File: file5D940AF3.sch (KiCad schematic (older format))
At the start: 42 parts, among them CN1 KEYBOARD_20PIN_MALE, CN2 USER_PORT_CON, CN4 SERIAL_BUS_CON, CN8 CONTROL_PORT, CN9 CONTROL_PORT, U1 CIA_U1, U2 CIA_U2, U20 556, U27 7408_U27, U28 4066_U28, U7 6510_MPU, U8 7406N

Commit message: schematics update
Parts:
- removed RP3: R_US_ARRAY, Resistor_THT:R_Array_SIP8, symbol KU-schematics-library:R_US_ARRAY
- added FB5: FERRITE_NARROW, KU-14194HB-RevB-KiCad:RECTIFIER, symbol KU-schematics-library:FERRITE_NARROW
- added RP3: R_ARRAY_7WAY_US, KU-14194HB-RevB-KiCad:RP_ARRAY_7WAY, symbol KU-schematics-library:R_ARRAY_7WAY_US
- added RP4: R_ARRAY_9WAY_US, KU-14194HB-RevB-KiCad:RP_ARRAY_9WAY, symbol KU-schematics-library:R_ARRAY_9WAY_US
- CN2: footprint (none) -> KU-14194HB-RevB-KiCad:EDGE_CON_24P
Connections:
- net labels added: A0, A0-A15, A1, A10, A11, A12, A13, A14, A15, A2, A3, A4, A5, A6, A7, A8, A9, D0, D1, D2, D3, D4, D5, D6, D7, DO-D7, PH2_FB, PHI2, RDY, R\~W~, ~CIA1~, ~CIA2~, ~IRQ~, ~VA14~, ~VA15~
- wire segments 291 -> 383
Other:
- note added: "RP4\n3.3K"

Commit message: more connectors and stuff
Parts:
- added C1, C103, C18, C59, C89, C92, C95, C98, C99: .1, KU-14194HB-RevB-KiCad:CAP_P5.08mm, symbol Device:C_Small
- added C100, C97: .22, KU-14194HB-RevB-KiCad:CAP_P5.08mm, symbol Device:C_Small
- added C102, C57: 10uF, KU-14194HB-RevB-KiCad:CAP_ELYT_RADIAL_P2.54mm, symbol Device:CP_Small
- added C19: 2200uF, KU-14194HB-RevB-KiCad:LARGE_ELECTROLYTIC_33x18_P38.10mm_AXIAL_TH, symbol Device:CP_Small
- added C20, C21: .22, KU-14194HB-RevB-KiCad:CAP_POLY_100V_TH_P10.16mm, symbol Device:C_Small
- added C88: 1000uF, KU-14194HB-RevB-KiCad:LARGE_ELECTROLYTIC_33x18_P38.10mm_AXIAL_TH, symbol Device:CP_Small
- added C90: 470uF, KU-14194HB-RevB-KiCad:LARGE_ELECTROLYTIC_33x18_P38.10mm_AXIAL_TH, symbol Device:CP_Small
- added C91: 100uF, KU-14194HB-RevB-KiCad:CAP_ELYT_RADIAL_P5.08mm, symbol Device:CP_Small
- added CN10: LED_CONNECTOR, symbol Connector_Generic:Conn_01x03
- added CN3: CASSETTE_PORT_CON, KU-14194HB-RevB-KiCad:EDGE_CON_12P_TAPE, symbol KU-schematics-library:CASSETTE_PORT_CON
- added CN7: POWER_CON, KU-14194HB-RevB-KiCad:POWER_CON_DIN7, symbol KU-schematics-library:POWER_CON
- added CR2: IN755, KU-14194HB-RevB-KiCad:ZENER_12.7mm, symbol Device:D_Zener_Small_ALT
- added CR4: BRIDGE_RECTIFIER, symbol KU-schematics-library:BRIDGE_RECTIFIER
- added CR5, CR6: 1N4001, KU-14194HB-RevB-KiCad:RECTIFIER_TH_P12.7mm, symbol Diode:1N4001
- added F1: 1A, symbol Device:Fuse
- added FB1, FB2, FB20, FB21, FB3: FERRITE_NARROW, KU-14194HB-RevB-KiCad:FERRITE_BEAD_TH_P12.7mm, symbol KU-schematics-library:FERRITE_NARROW
- added L4: CHOKE, symbol KU-schematics-library:CHOKE
- added L5: 1.2uH, symbol Device:L_Core_Iron
- added Q1, Q2: 2SC1815, KU-14194HB-RevB-KiCad:Q_NPN_ECB, symbol Transistor_BJT:2SC1815
- added Q3: TP298/2SD880, Package_TO_SOT_THT:TO-220-3_Vertical, symbol Transistor_BJT:TIP41
- added R1, R43, R44, R45: 3K3, KU-14194HB-RevB-KiCad:RESISTOR, symbol KU-schematics-library:R_US_CUSTOM
- added R2: 1.5K, KU-14194HB-RevB-KiCad:RESISTOR, symbol KU-schematics-library:R_US_CUSTOM
- added R3: 10K, KU-14194HB-RevB-KiCad:RESISTOR, symbol KU-schematics-library:R_US_CUSTOM
- added R39: 390, KU-14194HB-RevB-KiCad:RESISTOR, symbol KU-schematics-library:R_US_CUSTOM
- added R4: 1K, KU-14194HB-RevB-KiCad:RESISTOR, symbol KU-schematics-library:R_US_CUSTOM
- added SW1: POWER_SWITCH, symbol KU-schematics-library:POWER_SWITCH
- added VR1: 7812, KU-14194HB-RevB-KiCad:VOTLAGE_REGULATOR_TO220, symbol KU-schematics-library:7812
- added VR2: 7805, KU-14194HB-RevB-KiCad:VOTLAGE_REGULATOR_TO220, symbol KU-schematics-library:7805
- C8: footprint (none) -> KU-14194HB-RevB-KiCad:CAP_ELYT_RADIAL_P2.54mm
- CN1: footprint (none) -> KU-14194HB-RevB-KiCad:KEYBOARD_CON
- CN4: footprint (none) -> KU-14194HB-RevB-KiCad:SERIAL_CON_DIN6
- CN8, CN9: footprint (none) -> KU-14194HB-RevB-KiCad:JOYPORT_DB9
- FB18, FB5, FB7, FB8, FB9: footprint KU-14194HB-RevB-KiCad:RECTIFIER -> KU-14194HB-RevB-KiCad:FERRITE_BEAD_TH_P12.7mm
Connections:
- net labels added: +12V, +9V_UNREG, 5V_FB3, 5V_joyport, 9V_UNREG, CAEC, CAN+5V, CASS_MOTOR, CASS_SENSE, CASS_WRT, CASS_WRT', GND_LED, LED+, ~CHAREN~, ~HIRAM~, ~LORAM~
- wire segments 383 -> 540
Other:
- note added: "(6-PIN MALE EDGE)"
- note added: "(7PIN MALE DIN)"
- note added: "+5"
- note added: "100V"
- note added: "16V"
- note added: "50V"
- note added: "7.5V"
- note added: "9VAC"
- note added: "CASSETTE"
- note added: "LED CONNECTOR"
- note added: "POWER INPUT"
- moved on the sheet: C105, C24, C39, R34, R36, R50, U20B, U8F

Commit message: added missing parts. powre connector is upside down in the ku board
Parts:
- CN10: footprint (none) -> KU-14194HB-RevB-KiCad:LED_CON
- CR4: footprint (none) -> KU-14194HB-RevB-KiCad:BRIDGE_RECTIFIER
- F1: footprint (none) -> KU-14194HB-RevB-KiCad:FUSE
- L4: footprint (none) -> KU-14194HB-RevB-KiCad:CHOKE
- L5: footprint (none) -> KU-14194HB-RevB-KiCad:INDUCTOR_P15.24mm
- SW1: footprint (none) -> KU-14194HB-RevB-KiCad:POWER_SWITCH
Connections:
- net labels added: 9VAC
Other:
- note removed: "9VAC"
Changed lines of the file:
@@
 F 0 "CN10" V 9313 10876 118 0000 R CNN
 F 1 "LED_CONNECTOR" V 8972 10462 50  0001 R CNN
-F 2 "" H 9150 10650 50  0001 C CNN
+F 2 "KU-14194HB-RevB-KiCad:LED_CON" H 9150 10650 50  0001 C CNN
 F 3 "~" H 9150 10650 50  0001 C CNN
 	1    9150 10650
@@
 F 0 "L5" H 11288 9996 50  0000 L CNN
 F 1 "1.2uH" H 11288 9905 50  0000 L CNN
-F 2 "" H 11200 9950 50  0001 C CNN
+F 2 "KU-14194HB-RevB-KiCad:INDUCTOR_P15.24mm" H 11200 9950 50  0001 C CNN
 F 3 "~" H 11200 9950 50  0001 C CNN
 	1    11200 9950
@@
 F 0 "L4" H 10375 10037 50  0000 L CNN
 F 1 "CHOKE" H 10350 10050 50  0001 L CNN
-F 2 "" H 10300 9950 50  0001 C CNN
+F 2 "KU-14194HB-RevB-KiCad:CHOKE" H 10300 9950 50  0001 C CNN
 F 3 "" H 10300 9950 50  0001 C CNN
 	1    10300 9950
@@
 	10300 10650 10300 10200
 Connection ~ 10300 10200
-Wire Wire Line
-	10950 10650 11200 10650
-Connection ~ 11200 10650
 Connection ~ 10700 10200
 Wire Wire Line
@@
 L KU-schematics-library:POWER_SWITCH SW1
 U 1 1 5E38E46E
-P 10700 10650
-F 0 "SW1" H 10800 10800 50  0000 L CNN
-F 1 "POWER_SWITCH" H 11094 10768 50  0001 L CNN
-F 2 "" H 10700 10650 50  0001 C CNN
-F 3 "" H 10700 10650 50  0001 C CNN
-	1    10700 10650
-	1    0    0    -1
+P 10700 10400
+F 0 "SW1" H 10850 10550 50  0000 L CNN
+F 1 "POWER_SWITCH" H 11094 10518 50  0001 L CNN
+F 2 "KU-14194HB-RevB-KiCad:POWER_SWITCH" H 10700 10400 50  0001 C CNN
+F 3 "" H 10700 10400 50  0001 C CNN
+	1    10700 10400
+	1    0    0    1
 $EndComp
 Wire Wire Line
@@
 Text Label 10700 9500 1    50   ~ 0
 9VAC~~
-Text Notes 10700 10400 1    50   ~ 0
-9VAC
 Text Notes 11200 10400 1    50   ~ 0
 +5
@@
 F 0 "F1" H 10150 9469 50  0000 L CNN
 F 1 "1A" H 10150 9393 50  0000 L CNN
-F 2 "" V 10230 9400 50  0001 C CNN
+F 2 "KU-14194HB-RevB-KiCad:FUSE" V 10230 9400 50  0001 C CNN
 F 3 "~" H 10300 9400 50  0001 C CNN
 	1    10300 9400
@@
 F 0 "CR4" H 10450 8900 50  0000 L CNN
 F 1 "BRIDGE_RECTIFIER" H 10300 7850 50  0001 C CNN
-F 2 "" H 10300 8750 50  0001 C CNN
+F 2 "KU-14194HB-RevB-KiCad:BRIDGE_RECTIFIER" H 10300 8750 50  0001 C CNN
 F 3 "" H 10300 8750 50  0001 C CNN
 	1    10300 8750
@@
 Text Label 9250 10350 1    31   ~ 0
 LED+
+Text Label 1950 4000 0    31   ~ 0
+5V_joyport
+Text Label 9900 9250 0    50   ~ 0
+'9VAC~~
+Text Label 10700 10400 1    50   ~ 0
+9VAC
+Wire Wire Line
+	11300 10650 11200 10650
+Connection ~ 11200 10650
 Wire Bus Line
 	7750 7100 7750 7400
@@
 Wire Bus Line
 	7050 3550 7050 8400
-Text Label 1950 4000 0    31   ~ 0
-5V_joyport
 $EndSCHEMATC

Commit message: oscillator
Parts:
- added C107, C108: 10uF, KU-14194HB-RevB-KiCad:CAP_P5.08mm, symbol Device:C_Small
- added C36, C68: .1, KU-14194HB-RevB-KiCad:CAP_P5.08mm, symbol Device:C_Small
- added C70: ~, KU-14194HB-RevB-KiCad:CAP_P5.08mm, symbol Device:C_Small
- added C86: ?, KU-14194HB-RevB-KiCad:CAP_P5.08mm, symbol Device:C_Small
- added FB16, FB17: FERRITE_NARROW, KU-14194HB-RevB-KiCad:FERRITE_BEAD_TH_P12.7mm, symbol KU-schematics-library:FERRITE_NARROW
- added R101: ?, KU-14194HB-RevB-KiCad:RESISTOR, symbol KU-schematics-library:R_US_CUSTOM
- added R26: 100, KU-14194HB-RevB-KiCad:RESISTOR, symbol KU-schematics-library:R_US_CUSTOM
- added U31: 74LS629N, symbol KU-schematics-library:74LS629N
- added U? (x11): GND_SMALL, symbol KU-14194HB-REV-B-KiCad-rescue:GND_SMALL-power
- added Y1: Crystal, symbol KU-schematics-library:Crystal
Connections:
- net labels added: +Vc, DOT_CLOCK
- wire segments 540 -> 578
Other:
- moved on the sheet: C105, C24, C39, R34, R36, R50, U20B, U8F

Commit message: Oscillator area
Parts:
- removed R101: ?, KU-14194HB-RevB-KiCad:RESISTOR, symbol KU-schematics-library:R_US_CUSTOM
- removed U? (x11): GND_SMALL, symbol KU-14194HB-REV-B-KiCad-rescue:GND_SMALL-power
- added C56, C58, C66, C67, C74, C84: .1, KU-14194HB-RevB-KiCad:CAP_P5.08mm, symbol Device:C_Small
- added C65: 10uF, KU-14194HB-RevB-KiCad:CAP_ELYT_RADIAL_P2.54mm, symbol Device:C_Small
- added C83: 82pF, KU-14194HB-RevB-KiCad:RESISTOR, symbol Device:C_Small
- added C85: .47, KU-14194HB-RevB-KiCad:CAP_P5.08mm, symbol Device:C_Small
- added E1: JUMPER_WIRE, KU-14194HB-RevB-KiCad:JUMPER_WIRE, symbol KU-schematics-library:JUMPER_WIRE
- added FB19: FERRITE_NARROW, KU-14194HB-RevB-KiCad:FERRITE_BEAD_TH_P12.7mm, symbol KU-schematics-library:FERRITE_NARROW
- added L2: 2.2uH, symbol Device:L
- added Q7: 2SC1815, KU-14194HB-RevB-KiCad:Q_NPN_ECB, symbol Transistor_BJT:2SC1815
- added R16: 1K, KU-14194HB-RevB-KiCad:RESISTOR, symbol KU-schematics-library:R_US_CUSTOM
- added R17: 2K7, KU-14194HB-RevB-KiCad:RESISTOR, symbol KU-schematics-library:R_US_CUSTOM
- added R19: 15K, KU-14194HB-RevB-KiCad:RESISTOR, symbol KU-schematics-library:R_US_CUSTOM
- added R27: 500, KU-14194HB-RevB-KiCad:POTMETER, symbol KU-schematics-library:R_POTMETER_US
- added R52, R53: ?, KU-14194HB-RevB-KiCad:RESISTOR, symbol KU-schematics-library:R_US_CUSTOM
- added U29: 74LS74, KU-14194HB-RevB-KiCad:DIP14, symbol KU-schematics-library:74LS74
- added U30: 74LS193, KU-14194HB-RevB-KiCad:DIP16, symbol KU-schematics-library:74LS193
- added U32: MC4044, KU-14194HB-RevB-KiCad:DIP14, symbol KU-schematics-library:MC4044
- C107, C108: footprint KU-14194HB-RevB-KiCad:CAP_P5.08mm -> KU-14194HB-RevB-KiCad:CAP_ELYT_RADIAL_P2.54mm
- C36, C70, C86: footprint KU-14194HB-RevB-KiCad:CAP_P5.08mm -> KU-14194HB-RevB-KiCad:RESISTOR
- U31: footprint (none) -> KU-14194HB-RevB-KiCad:DIP16
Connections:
- net +Vc: now also U31.16 (VCC), C56.1, C67.1, C74.1, C84.1, E1.1, FB19.2, Q7.2 (C), R16.1, R53.1, U29.10, U29.13, U29.14, U30.15 (A), U30.16 (VCC), U30.4 (CNT_DN), U32.14
- net CAN+5V: now also C65.1, C66.1, L2.1
- net Earth: now also U31.3, C56.2, C58.2, C65.2, C66.2, C67.2, C74.2, C83.2, C84.2, E1.2, R52.2, U29.1, U29.2 (D), U29.3 (CK), U29.7, U30.14 (CLR), U30.8 (GND), U32.7
- net PHI_0: now reaches U7.1 (PH0IN)
- net PHI_0: now also U32.3
- net at U31.2 (FC): now also R16.2, R17.1, U32.8
- net at U31.4 (CX1): now also C86.2
- net at U31.5 (CX2): now also C86.1
- net at U31.1 (FC): now also C108.1, C58.1, R27.3
- net at U31.12: now also Y1.1
- net at U31.13: now also C70.2
- net at U31.15: now also C107.1, R26.2
- net PHI_COLOR: now reaches FB16.2
- net PHI_COLOR: now also U30.5 (CNT_UP)
- new net: R27.1, R53.2
- new net: R27.2, R52.1
- new net: FB19.1, L2.2
- new net: Q7.1 (E), U32.9
- new net: C85.2, Q7.3 (B), R19.1
- new net: C83.1, U30.11 (LOAD), U30.12 (CRY)
- new net: U29.5 (Q), U30.9 (D)
- new net: R19.2, U32.10, U32.5
- new net: U29.12 (D), U29.8 (~Q~)
- new net: U29.9 (Q), U32.1
- new net: C85.1, R17.2
- new net: U32.13, U32.4
- new net: U32.11, U32.2
- new net F_DIV: U29.11 (CK), U30.6 (Qc)
- new net jumper_select: E1.C, U29.4, U30.1 (B), U30.10 (C)
- no-connect marks 3 -> 8
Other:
- note added: "E1"
- note added: "E2"
- note added: "E3"
- note added: "No R101"
- moved on the sheet: C107, C108, C36, C68, C70, C86, FB16, FB17, R26, U31A, U31B, Y1

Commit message: More schematics
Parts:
- L2: footprint (none) -> KU-14194HB-RevB-KiCad:RESISTOR
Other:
- note added: "( 14.31818 MHz - NTSC )\n( 17.734472 MHz - PAL )"
- note added: "To Cartridge Expansion"
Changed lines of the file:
@@
 ~VA14~
 Text GLabel 7750 8900 2    50   Output ~ 0
-A0-A15
-Text GLabel 7750 8400 2    50   Output ~ 0
-DO-D7
+A[0..15]
 Wire Wire Line
 	6850 7600 6950 7600
@@
 Wire Bus Line
 	7750 8400 7050 8400
-Wire Bus Line
-	7750 8900 7150 8900
 Entry Wire Line
 	7050 1850 7150 1950
@@
 	7350 4350 6850 4350
 Connection ~ 7350 6700
-Entry Wire Line
-	7050 8500 7150 8600
-Entry Wire Line
-	7050 8600 7150 8700
-Entry Wire Line
-	7050 8700 7150 8800
-Entry Wire Line
-	7050 8800 7150 8900
-Wire Wire Line
-	6850 8500 7050 8500
-Wire Wire Line
-	6850 8600 7050 8600
-Wire Wire Line
-	6850 8700 7050 8700
-Wire Wire Line
-	6850 8800 7050 8800
 Text Label 6900 8800 0    50   ~ 0
 A0
@@
 A3
 Entry Wire Line
-	7050 5900 7150 6000
+	7100 5900 7200 6000
 Entry Wire Line
-	7050 6000 7150 6100
+	7100 6000 7200 6100
 Entry Wire Line
-	7050 6100 7150 6200
+	7100 6100 7200 6200
 Entry Wire Line
-	7050 6200 7150 6300
+	7100 6200 7200 6300
 Wire Wire Line
-	6850 5900 7050 5900
+	6850 5900 7100 5900
 Wire Wire Line
-	6850 6000 7050 6000
+	6850 6000 7100 6000
 Wire Wire Line
-	6850 6100 7050 6100
+	6850 6100 7100 6100
 Wire Wire Line
-	6850 6200 7050 6200
+	6850 6200 7100 6200
 Text Label 6900 6200 0    50   ~ 0
 A0
@@
 	6950 4300 7100 4300
 Wire Wire Line
-	7100 4300 7100 4250
+	7100 4300 7050 4250
 Wire Wire Line
-	7100 4250 7200 4250
+	7050 4250 7200 4250
 Wire Wire Line
 	7450 4250 7400 4250
@@
 Entry Wire Line
 	7750 7400 7850 7300
-Wire Bus Line
-	7750 7400 7150 7400
-Connection ~ 7150 7400
 $Comp
 L KU-schematics-library:R_ARRAY_9WAY_US RP4
@@
 F 0 "L2" V 9485 2998 50  0000 C CNN
 F 1 "2.2uH" V 9414 2956 50  0000 C CNN
-F 2 "" H 9350 2950 50  0001 C CNN
+F 2 "KU-14194HB-RevB-KiCad:RESISTOR" H 9350 2950 50  0001 C CNN
 F 3 "~" H 9350 2950 50  0001 C CNN
 	1    9350 2950
@@
 Wire Wire Line
 	11050 4000 11200 4000
-Wire Bus Line
-	7750 7100 7750 7400
-Wire Bus Line
-	7150 7400 7150 8900
-Wire Bus Line
-	7150 1950 7150 7400
-Wire Bus Line
-	7050 3550 7050 8400
 Connection ~ 11200 4000
 Wire Wire Line
@@
 P 11200 4200
 AR Path="/605F81BA" Ref="#U?"  Part="1"
-AR Path="/5D940AF4/605F81BA" Ref="#U?"  Part="1"
-F 0 "#U?" H 11200 4200 50  0001 C CNN
+AR Path="/5D940AF4/605F81BA" Ref="#U0151"  Part="1"
+F 0 "#U0151" H 11200 4200 50  0001 C CNN
 F 1 "GND_SMALL" H 11200 4200 50  0001 C CNN
 F 2 "" H 11200 4200 50  0001 C CNN
@@
 	1    0    0    -1
 $EndComp
+Text Notes 9600 4950 0    39   ~ 0
+( 14.31818 MHz - NTSC )\n( 17.734472 MHz - PAL )
+Wire Wire Line
+	5350 10500 5350 10950
+Wire Wire Line
+	5350 10950 5550 10950
+Connection ~ 5350 10500
+Text GLabel 5550 10950 2    50   Input ~ 0
+~NMI~
+Text Notes 5350 11100 0    39   ~ 0
+To Cartridge Expansion
+Wire Wire Line
+	6850 8800 7050 8800
+Wire Wire Line
+	6850 8700 7050 8700
+Wire Wire Line
+	6850 8600 7050 8600
+Wire Wire Line
+	6850 8500 7050 8500
+Wire Bus Line
+	7750 8900 7150 8900
+Wire Bus Line
+	7750 7400 7150 7400
+Entry Wire Line
+	7050 8800 7150 8900
+Entry Wire Line
+	7050 8700 7150 8800
+Entry Wire Line
+	7050 8600 7150 8700
+Entry Wire Line
+	7050 8500 7150 8600
+Wire Bus Line
+	7150 5900 7200 5900
+Wire Bus Line
+	7200 6350 7150 6350
+Wire Bus Line
+	7150 6350 7150 7400
+Connection ~ 7150 7400
+Text GLabel 7750 8400 2    39   BiDi ~ 0
+D[0..7]
+Wire Bus Line
+	7750 7100 7750 7400
+Wire Bus Line
+	7150 7400 7150 8900
+Wire Bus Line
+	7200 5900 7200 6350
+Wire Bus Line
+	7150 1950 7150 5900
+Wire Bus Line
+	7050 3550 7050 8400
 $EndSCHEMATC

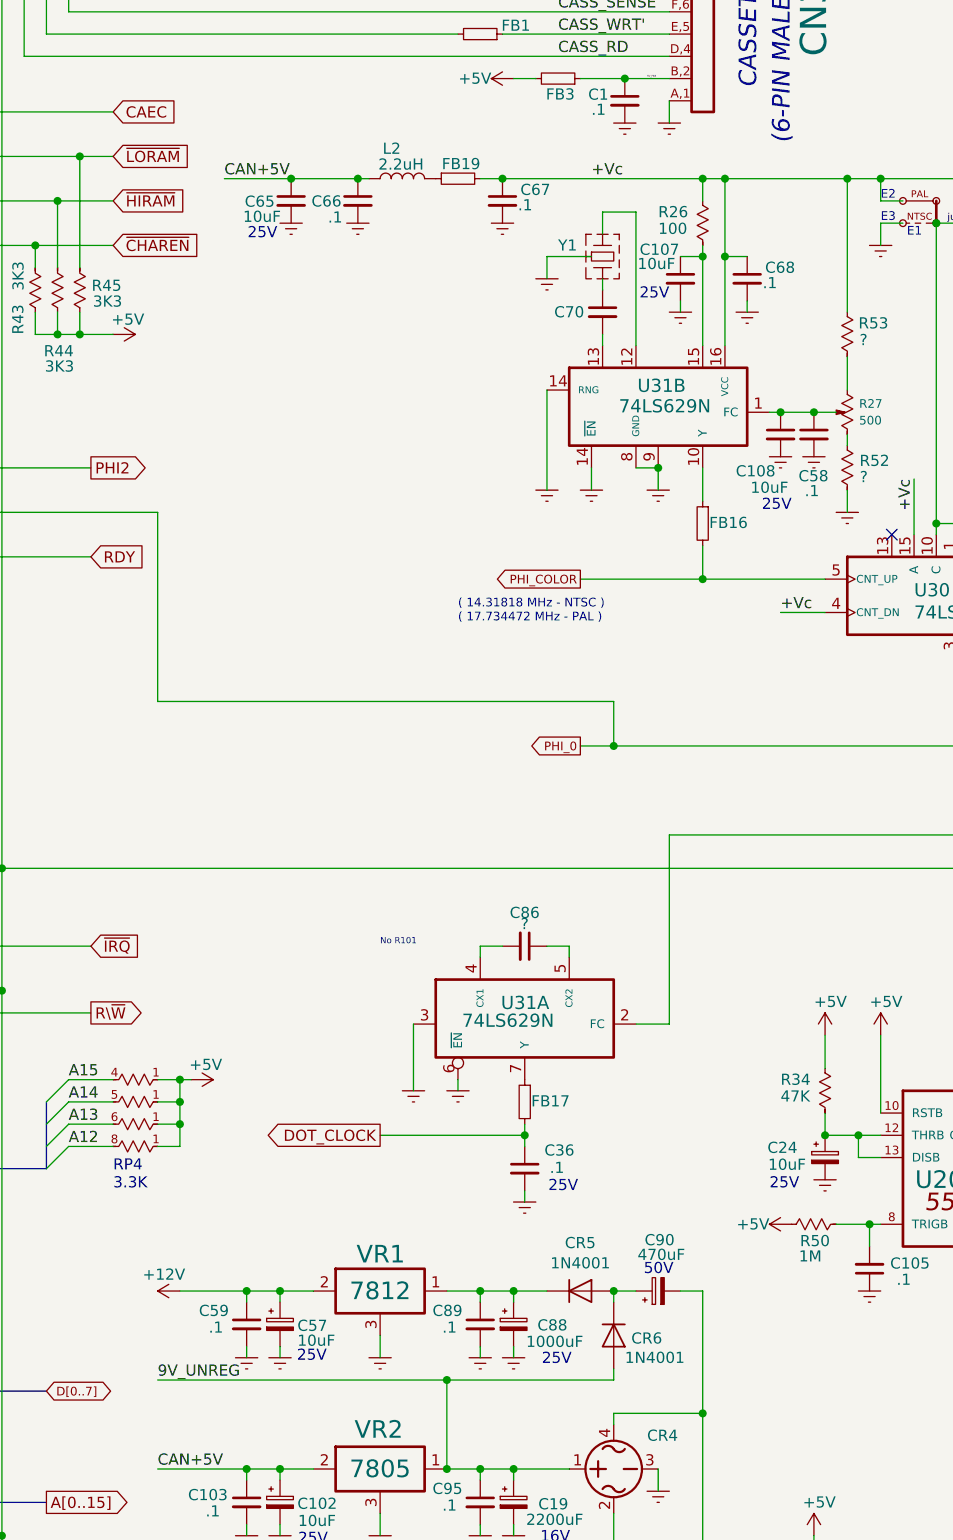
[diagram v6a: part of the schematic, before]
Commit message: Tighter ram symbols. Getting closer to the end of the schematics.
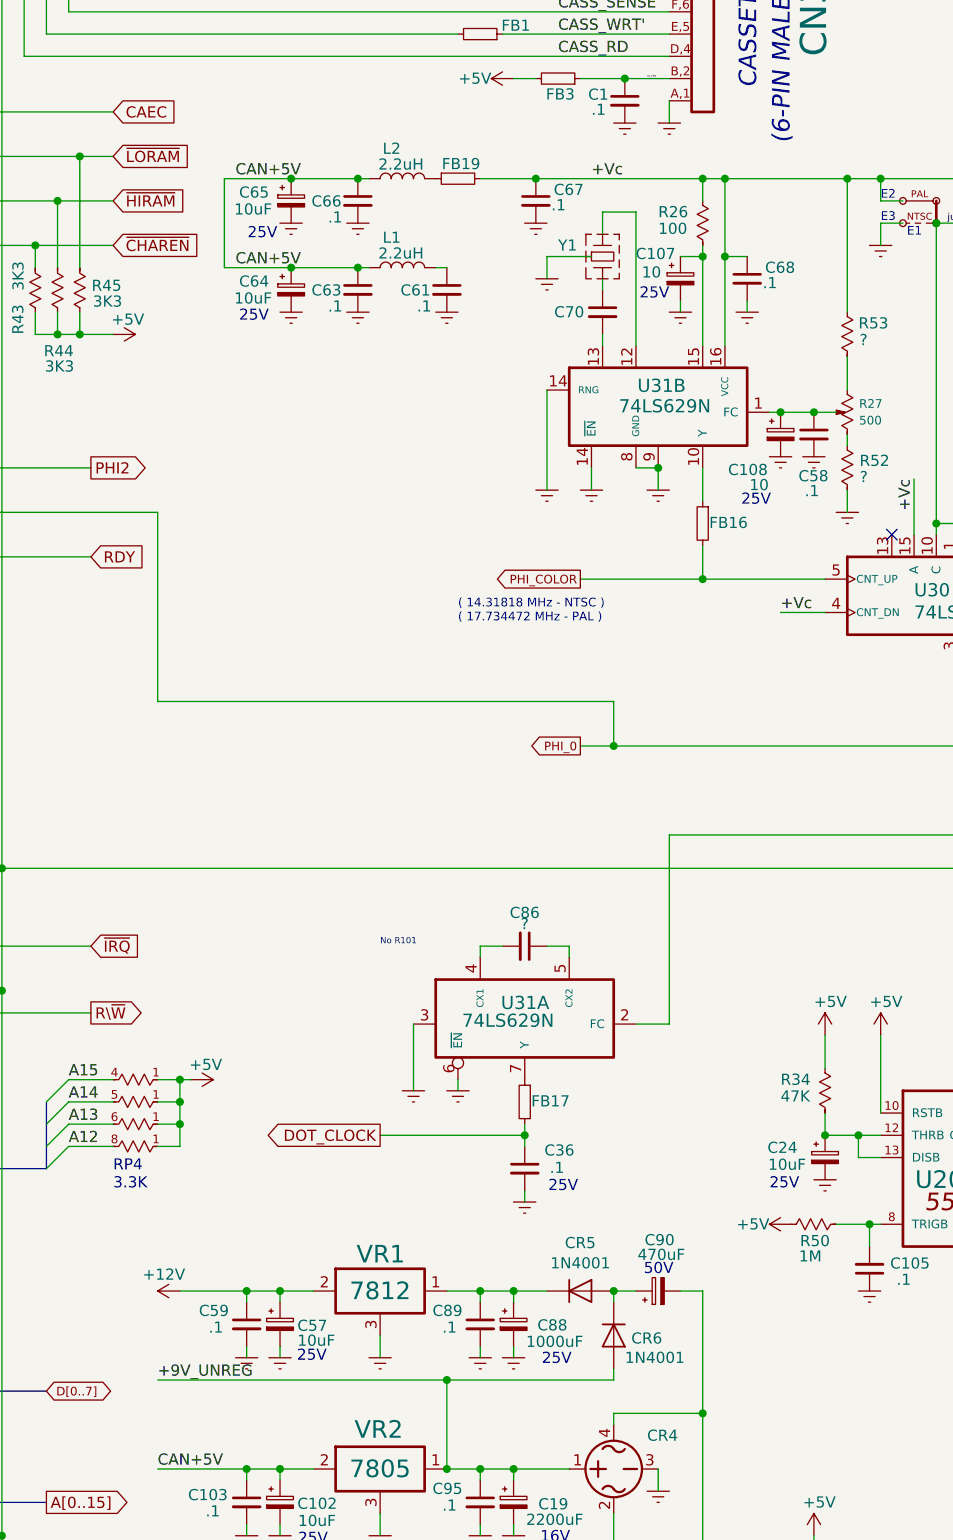
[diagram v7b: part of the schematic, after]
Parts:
- removed C107, C108, C65: 10uF, KU-14194HB-RevB-KiCad:CAP_ELYT_RADIAL_P2.54mm, symbol Device:C_Small
- added C107, C108: 10, KU-14194HB-RevB-KiCad:CAP_ELYT_RADIAL_P2.54mm, symbol Device:CP_Small
- added C61, C63: .1, KU-14194HB-RevB-KiCad:CAP_P5.08mm, symbol Device:C_Small
- added C64, C65: 10uF, KU-14194HB-RevB-KiCad:CAP_ELYT_RADIAL_P2.54mm, symbol Device:CP_Small
- added L1: 2.2uH, KU-14194HB-RevB-KiCad:RESISTOR, symbol Device:L
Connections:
- net 9V_UNREG is gone; now on net +9V_UNREG: C19.1, C95.1, CR4.1, CR6.2 (A), VR2.1
- net CAN+5V: now also C63.1, C64.1, C65.1, L1.1
- net Earth: now also C107.2, C108.2, C61.2, C63.2, C64.2, C65.2
- net at C58.1, R27.3, U31.1 (FC): now also C108.1
- net at R26.2, U31.15: now also C107.1
- new net: C61.1, L1.2
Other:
- moved on the sheet: C67

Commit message: Almost done now
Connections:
- net PHI_0 renamed PHI0
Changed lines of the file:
@@
 	1    0    0    -1
 $EndComp
-Text GLabel 10150 4750 0    39   Output ~ 0
+Text GLabel 10150 4750 0    50   Output ~ 0
 PHI_COLOR
 Wire Wire Line
@@
 Wire Wire Line
 	13500 5500 10300 5500
-Text GLabel 10150 5500 0    39   Output ~ 0
-PHI_0
+Text GLabel 10150 5500 0    50   Output ~ 0
+PHI0
 Wire Wire Line
 	10300 5500 10300 5300
@@
 	1    0    0    -1
 $EndComp
+Text Label 8500 6400 0    50   ~ 0
+CAN+5V
 Wire Bus Line
 	7750 7100 7750 7400
